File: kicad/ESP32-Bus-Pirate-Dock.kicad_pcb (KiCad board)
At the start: 2 copper layers, 95.3 x 74.8 mm, 21 parts, among them J1 Conn_01x10V, J2 Conn_01x22, J3 Conn_01x22, J4 Conn_01x10H, U1 ESP32-S3-DEVKITC-1-N8R2, U2 AMS1117-1.8, U3 FXMA108

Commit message: Added logo
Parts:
- added G***: LOGO, LOGO, F.Cu at (193.8, 116.0)
- SW_1: value SW_BOOT -> BOOT
- moved C3 51.5 mm to (192.6, 90.2)
- moved C2 49.2 mm to (189.2, 86.4)
- moved U2 49.2 mm to (194.8, 83.6)
- moved C1 47.5 mm to (196.6, 90.2), turned to 0 degrees
- moved C4 45.1 mm to (189.2, 81.2), turned to 90 degrees
- moved H2 10.1 mm to (205.0, 53.8)
- moved H4 10.1 mm to (205.4, 120.1)
- moved D2 8.90 mm to (188.3, 62.5)
- moved S1 8.90 mm to (188.2, 54.7)
- moved D1 8.90 mm to (192.4, 62.5)
- moved D3 8.90 mm to (184.2, 62.5)
- moved R1 8.90 mm to (198.6, 56.6)
- moved SW_1 7.01 mm to (194.6, 105.3)
- moved U1 2.46 mm to (162.2, 93.3)
- moved U3 2.46 mm to (138.4, 90.9)
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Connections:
- U3 pad 11: unconnected-(U3-~{OE}-Pad11) -> GND
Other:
- board size 95.3 x 74.8 mm -> 85.4 x 74.8 mm

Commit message: First wiring attempt
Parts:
- moved H1 10.6 mm to (129.3, 64.4)
- moved R1 10.6 mm to (198.5, 67.2)
- moved H2 10.6 mm to (204.9, 64.4)
- moved S1 10.6 mm to (188.1, 65.2)
- moved D1 10.4 mm to (192.4, 72.9)
- moved D2 10.4 mm to (188.3, 72.9)
- moved D3 10.4 mm to (184.2, 72.9)
- moved G*** 3.56 mm to (192.2, 119.1)
- moved J3 0.91 mm to (146.9, 63.3)
- moved H3 0.68 mm to (129.1, 120.4)
- moved J2 0.64 mm to (177.4, 63.3)
- moved H4 0.14 mm to (205.3, 120.2)
- moved J4 0.09 mm to (127.2, 80.7)
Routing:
- net +5V: track 0.00 -> 93.6 mm
- net VTARGET: track 0.00 -> 91.0 mm, vias 0 -> 2
- net +1V8: track 0.00 -> 35.6 mm
- net GPIO0: track 0.00 -> 26.7 mm
- net GPIO13: track 0.00 -> 23.2 mm
- net GPIO12: track 0.00 -> 22.0 mm
- net GPIO11: track 0.00 -> 19.9 mm
- net GPIO10: track 0.00 -> 18.7 mm
- net IO13: track 0.00 -> 15.5 mm
- net GPIO15: track 0.00 -> 15.2 mm
- net IO12: track 0.00 -> 13.8 mm
- net GPIO16: track 0.00 -> 13.6 mm
- net IO15: track 0.00 -> 13.0 mm
- net GPIO17: track 0.00 -> 12.7 mm
- net GPIO18: track 0.00 -> 11.9 mm
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- added copper zone on B.Cu, net +3.3V
- added copper zone on F.Cu, net +3.3V
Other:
- board size 85.4 x 74.8 mm -> 85.4 x 64.8 mm

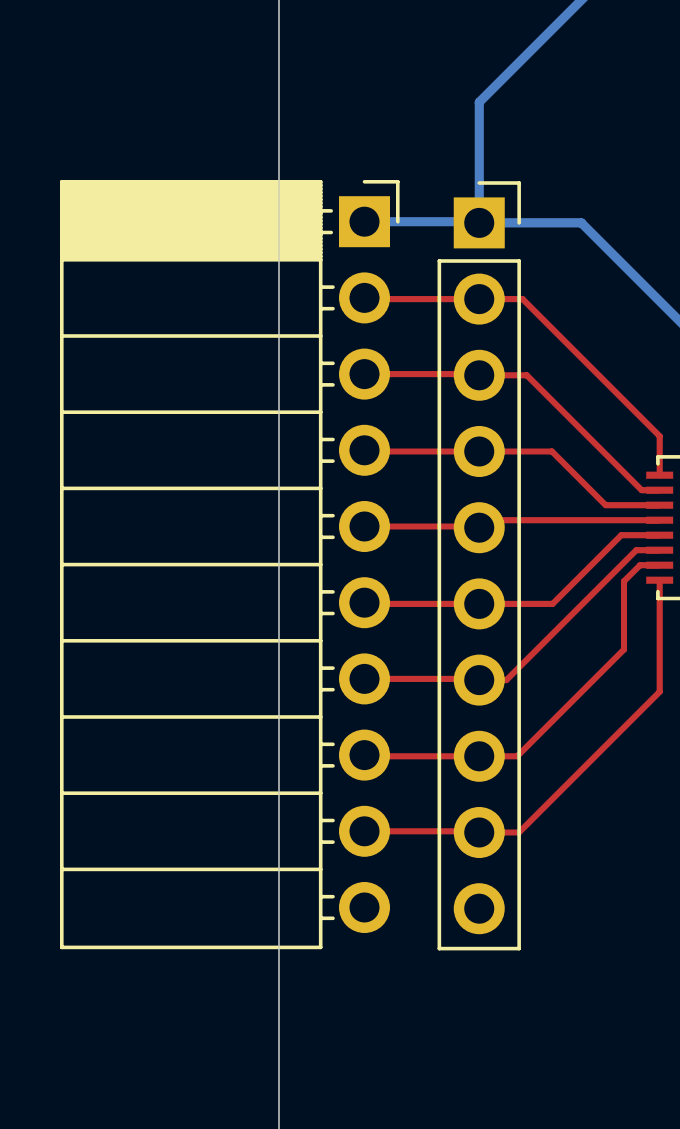
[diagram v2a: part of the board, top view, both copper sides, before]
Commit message: Excluded vertical header
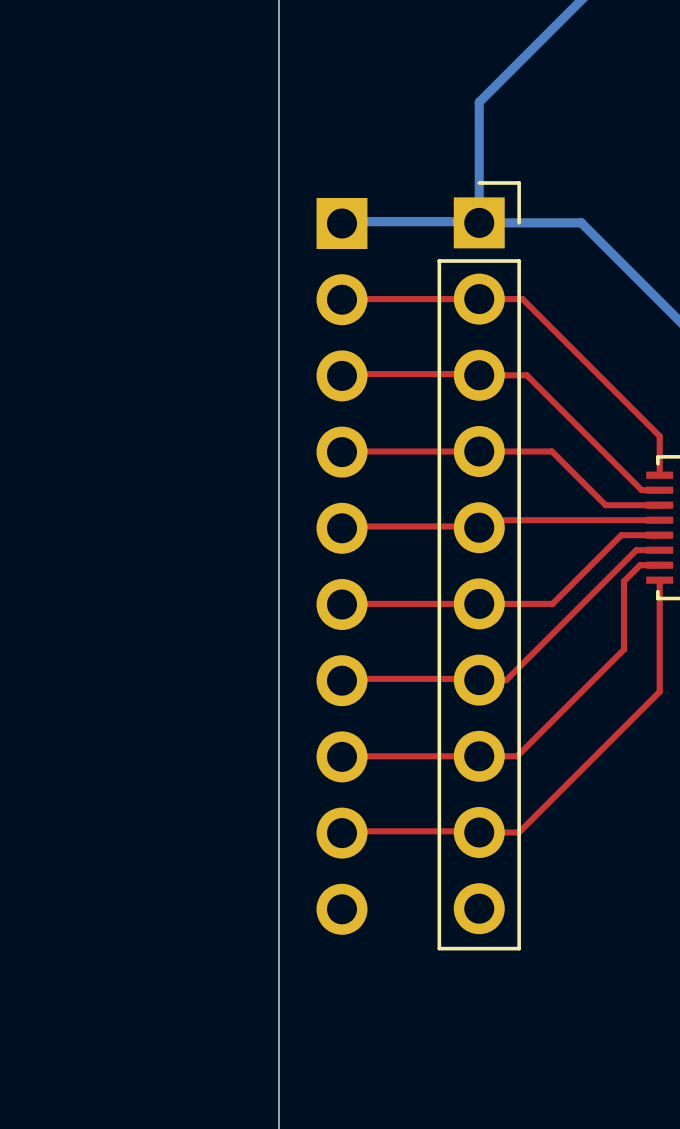
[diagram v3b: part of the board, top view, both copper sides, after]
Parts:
- J4: footprint Connector_PinSocket_2.54mm:PinSocket_1x10_P2.54mm_Horizontal -> Connector_PinHeader_2.54mm:PinHeader_1x10_P2.54mm_Horizontal; moved to B.Cu
- SW_1: value BOOT -> SW_BOOT
- moved J4 0.75 mm to (126.5, 80.8), turned to 180 degrees

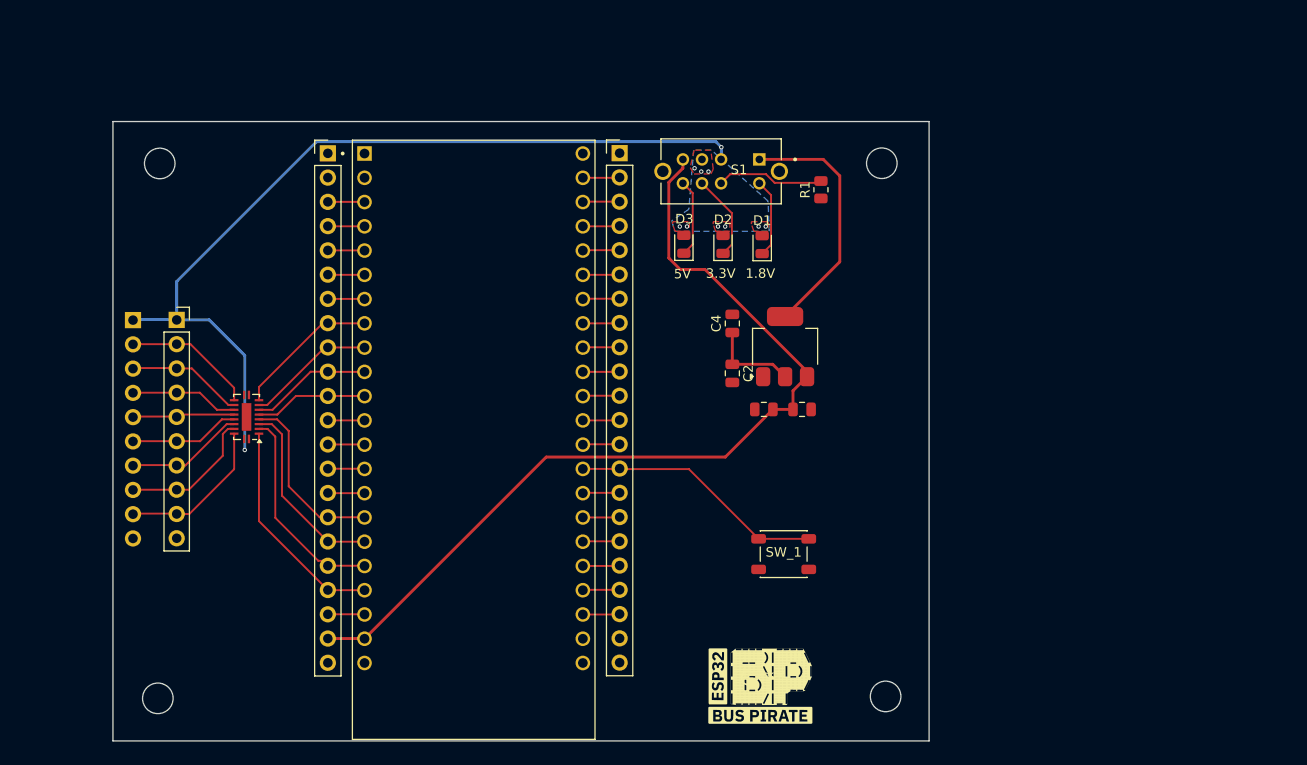
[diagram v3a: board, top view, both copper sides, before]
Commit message: Added keyed connector
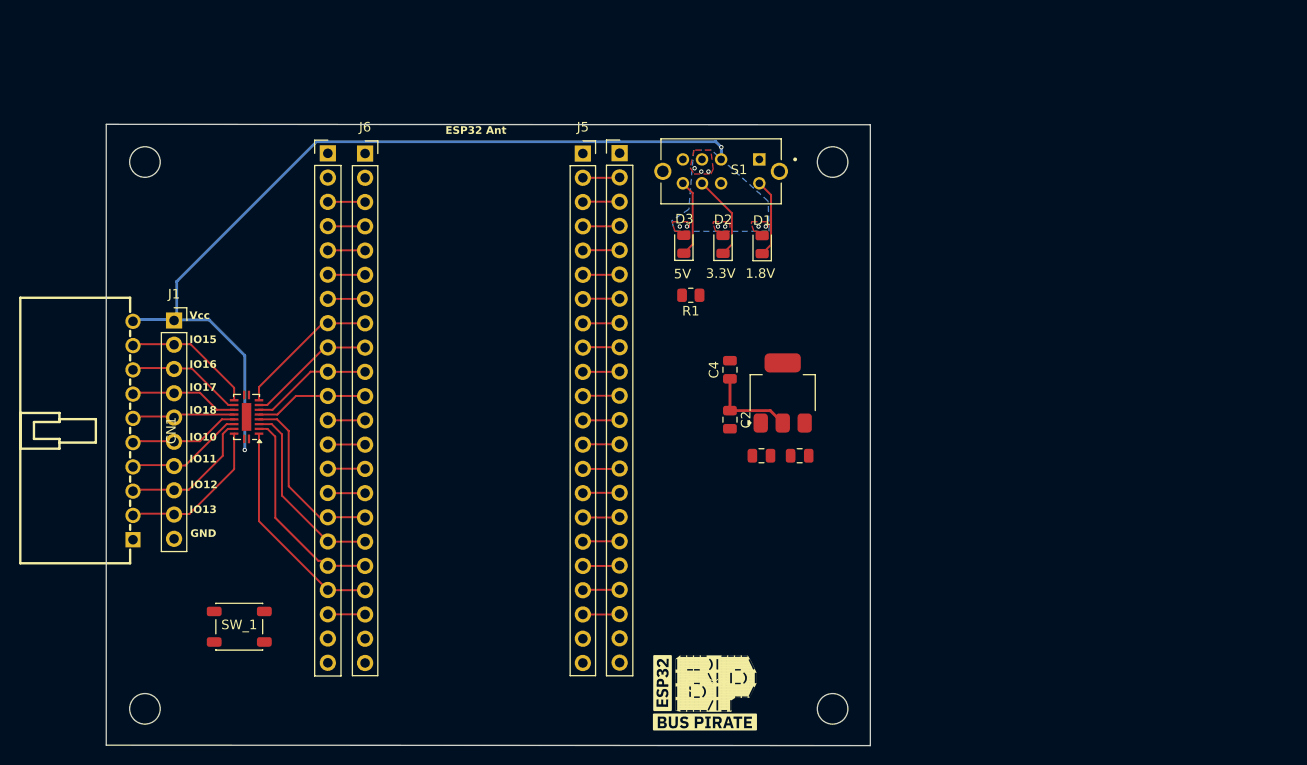
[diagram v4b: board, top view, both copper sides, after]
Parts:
- removed J4: Conn_01x10H, Connector_PinHeader_2.54mm:PinHeader_1x10_P2.54mm_Horizontal
- removed U1: ESP32-S3-DEVKITC-1-N8R2, ESP32-S3-DEVKITC-1-N8R2:XCVR_ESP32-S3-DEVKITC-1-N8R2
- added CN1: HX25418-10WA, HX25418:CONN-TH_HX25418-10WA, F.Cu at (126.5, 92.4)
- added J5: Conn_01x22, Connector_PinSocket_2.54mm:PinSocket_1x22_P2.54mm_Vertical, F.Cu at (173.6, 63.4)
- added J6: Conn_01x22, Connector_PinSocket_2.54mm:PinSocket_1x22_P2.54mm_Vertical, F.Cu at (150.8, 63.4)
- moved SW_1 57.5 mm to (137.6, 112.9)
- moved R1 17.5 mm to (184.9, 78.2), turned to 180 degrees
- moved G*** 5.84 mm to (186.4, 119.8)
- moved H4 5.70 mm to (199.8, 121.5)
- moved H2 5.15 mm to (199.8, 64.2)
- moved C1 4.86 mm to (196.3, 95.0)
- moved C2 4.86 mm to (189.0, 91.2)
- moved C3 4.86 mm to (192.3, 95.0)
- moved C4 4.86 mm to (189.0, 86.0)
- moved U2 4.86 mm to (194.5, 88.4)
- moved H3 1.74 mm to (127.8, 121.5)
- moved H1 1.56 mm to (127.8, 64.2)
- moved J1 0.28 mm to (130.8, 80.8)
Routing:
- net +5V: track 93.6 -> 0.00 mm
- net +1V8: track 35.6 -> 9.39 mm
- net GPIO0: track 26.7 -> 3.95 mm
- net Net-(R1-Pad2): track 11.3 -> 0.00 mm
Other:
- board size 85.4 x 64.8 mm -> 80 x 65 mm
- board text added: "ESP32 Ant"
- board text added: "GND"
- board text added: "IO10"
- board text added: "IO11"
- board text added: "IO12"
- board text added: "IO13"
- board text added: "IO15"
- board text added: "IO16"
- board text added: "IO17"
- board text added: "IO18"
- board text added: "Vcc"

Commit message: Fully routed PCB prototype
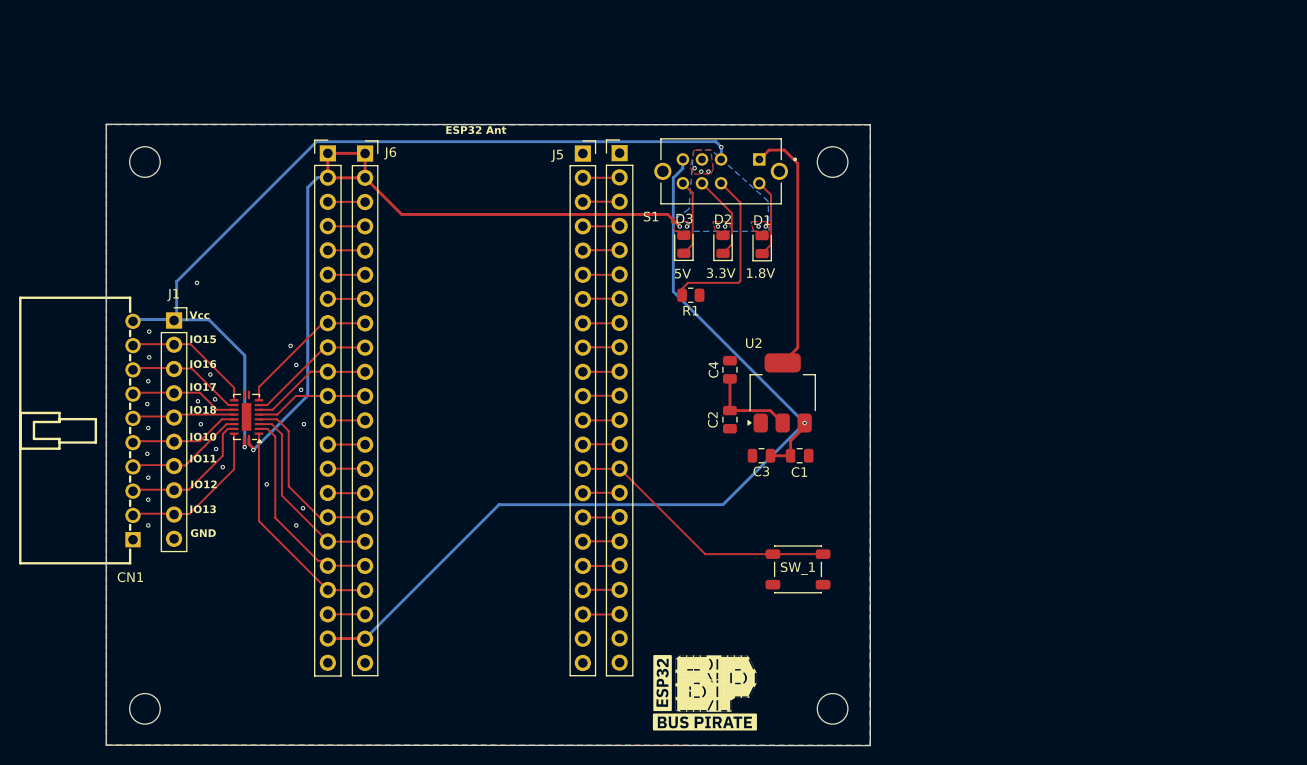
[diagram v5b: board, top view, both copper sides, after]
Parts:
- moved SW_1 58.8 mm to (196.1, 106.9)
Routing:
- net +5V: track 0.00 -> 99.1 mm, vias 0 -> 1
- net +3.3V: track 0.00 -> 81.7 mm, vias 9 -> 10
- net +1V8: track 9.39 -> 35.9 mm
- net GPIO0: track 3.95 -> 28.9 mm
- net Net-(R1-Pad2): track 0.00 -> 18.2 mm
- net VTARGET: track 91.0 -> 91.6 mm
- net GND: vias 0 -> 23
- added copper zone on B.Cu, net GND
- added copper zone on F.Cu, net GND

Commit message: DRC Check Passed
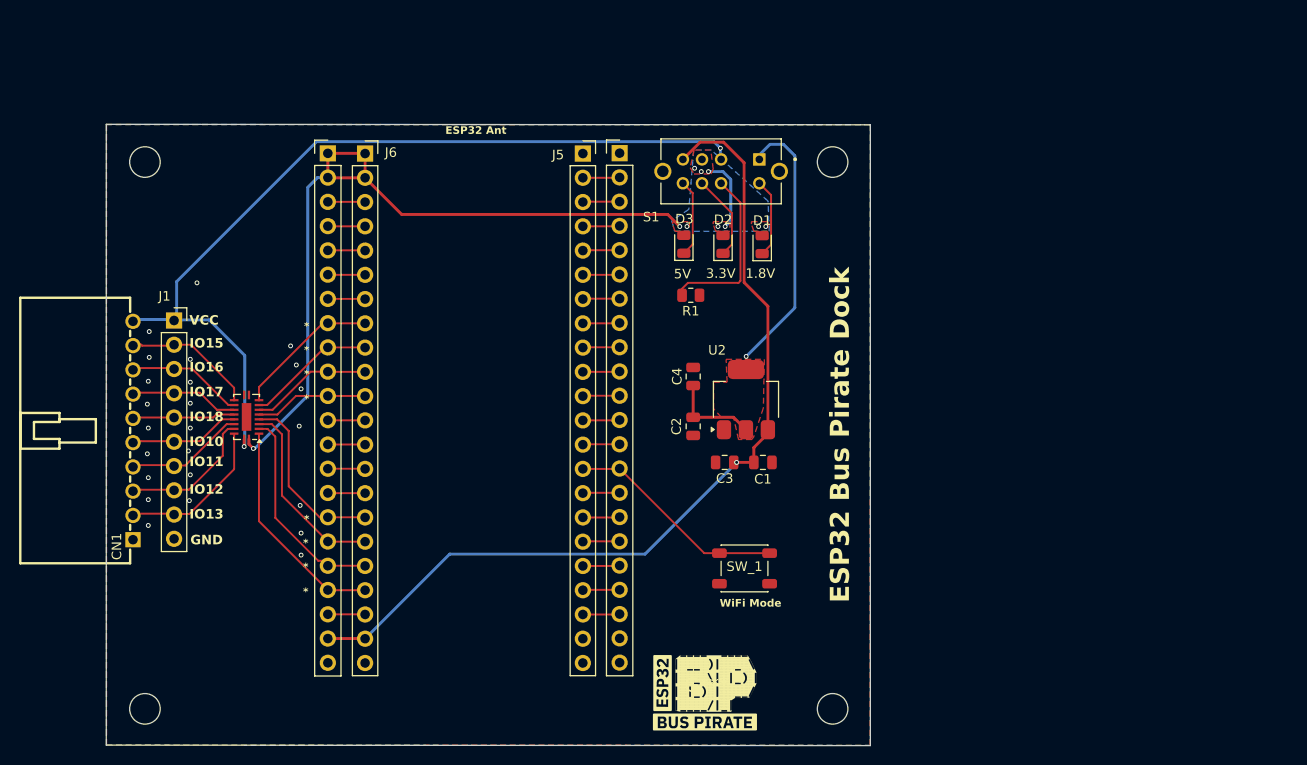
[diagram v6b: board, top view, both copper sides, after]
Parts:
- moved SW_1 5.60 mm to (190.5, 106.8)
- moved C1 3.91 mm to (192.4, 95.7)
- moved C3 3.91 mm to (188.4, 95.7)
- moved C2 3.91 mm to (185.2, 91.9)
- moved C4 3.91 mm to (185.2, 86.7)
- moved U2 3.91 mm to (190.7, 89.1)
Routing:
- net +3.3V: track 81.7 -> 89.3 mm
- net GPIO0: track 28.9 -> 23.2 mm
- net +5V: track 99.1 -> 93.6 mm
- net +1V8: track 35.9 -> 39.0 mm, vias 0 -> 1
- net IO18: track 9.96 -> 10.8 mm
- net GND: vias 23 -> 24
- added copper zone on F.Cu, net +1V8
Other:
- board text added: "*"
- board text added: "ESP32 Bus Pirate Dock"
- board text added: "VCC"
- board text added: "WiFi Mode"
- board text removed: "Vcc"

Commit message: Fixed connector polarity
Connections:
- CN1 pad 1: GND -> VTARGET
- CN1 pad 10: VTARGET -> GND
- J1 pad 1: VTARGET -> GND
- J1 pad 10: GND -> VTARGET
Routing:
- net VTARGET: track 91.4 -> 99.6 mm, vias 2 -> 1
- net GND: vias 24 -> 30
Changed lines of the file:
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@@
 			(layers "*.Cu" "*.Mask")
 			(remove_unused_layers no)
-			(net 10 "GND")
+			(net 43 "VTARGET")
 			(pinfunction "1")
 			(pintype "unspecified")
@@
 			(layers "*.Cu" "*.Mask")
 			(remove_unused_layers no)
-			(net 43 "VTARGET")
+			(net 10 "GND")
 			(pinfunction "10")
 			(pintype "unspecified")
@@
 			(layers "*.Cu" "*.Mask")
 			(remove_unused_layers no)
-			(net 43 "VTARGET")
+			(net 10 "GND")
 			(pinfunction "Pin_1")
 			(pintype "passive")
@@
 			(layers "*.Cu" "*.Mask")
 			(remove_unused_layers no)
-			(net 10 "GND")
+			(net 43 "VTARGET")
 			(pinfunction "Pin_10")
 			(pintype "passive")
@@
 	)
 	(gr_text "GND"
-		(at 132.5 104.4 0)
+		(at 132.5 81.5 0)
 		(layer "F.SilkS")
 		(effects
@@
 	)
 	(gr_text "VCC"
-		(at 132.4 81.4 0)
+		(at 132.5 104.1 0)
 		(layer "F.SilkS")
 		(effects
@@
 	)
 	(via
+		(at 157.3 66.6)
+		(size 0.5032)
+		(drill 0.3)
+		(layers "F.Cu" "B.Cu")
+		(free yes)
+		(net 10)
+	)
+	(via
 		(at 144 100.2)
 		(size 0.5032)
@@
 	)
 	(via
+		(at 169.2 62.8)
+		(size 0.5032)
+		(drill 0.3)
+		(layers "F.Cu" "B.Cu")
+		(free yes)
+		(net 10)
+	)
+	(via
 		(at 144.1 105.4)
 		(size 0.5032)
@@
 	)
 	(via
+		(at 156.8 100.1)
+		(size 0.5032)
+		(drill 0.3)
+		(layers "F.Cu" "B.Cu")
+		(free yes)
+		(net 10)
+	)
+	(via
 		(at 128.1 92.1)
 		(size 0.5032)
@@
 	)
 	(via
+		(at 156.015796 82.394434)
+		(size 0.5032)
+		(drill 0.3)
+		(layers "F.Cu" "B.Cu")
+		(free yes)
+		(net 10)
+	)
+	(via
 		(at 132.5 84.9)
 		(size 0.5032)
@@
 	)
 	(via
+		(at 168.8 72.1)
+		(size 0.5032)
+		(drill 0.3)
+		(layers "F.Cu" "B.Cu")
+		(free yes)
+		(net 10)
+	)
+	(via
+		(at 168.5 90.9)
+		(size 0.5032)
+		(drill 0.3)
+		(layers "F.Cu" "B.Cu")
+		(free yes)
+		(net 10)
+	)
+	(via
 		(at 143.9 91.9)
 		(size 0.5032)
@@
 	)
 	(segment
-		(start 138.14 94.04)
-		(end 138.14 93.24)
+		(start 126.59 103.7)
+		(end 126.5 103.79)
 		(width 0.3048)
 		(layer "F.Cu")
 		(net 43)
 	)
-	(via
-		(at 138.14 94.04)
-		(size 0.5032)
-		(drill 0.3)
-		(layers "F.Cu" "B.Cu")
-		(free yes)
-		(net 43)
-	)
-	(via
-		(at 188 62.8)
-		(size 0.5032)
-		(drill 0.3)
-		(layers "F.Cu" "B.Cu")
-		(free yes)
+	(segment
+		(start 138.14 101.96)
+		(end 138.14 96.2)
+		(width 0.3048)
+		(layer "F.Cu")
 		(net 43)
 	)
 	(segment
-		(start 188 63.9)
-		(end 188.075 63.975)
+		(start 136.4 103.7)
+		(end 138.14 101.96)
 		(width 0.3048)
-		(layer "B.Cu")
+		(layer "F.Cu")
 		(net 43)
 	)
 	(segment
-		(start 138.14 94.04)
-		(end 138.2 93.98)
+		(start 130.8 103.7)
+		(end 126.59 103.7)
 		(width 0.3048)
-		(layer "B.Cu")
+		(layer "F.Cu")
 		(net 43)
 	)
 	(segment
-		(start 188 62.8)
-		(end 188 63.9)
+		(start 130.8 103.7)
+		(end 136.4 103.7)
 		(width 0.3048)
-		(layer "B.Cu")
+		(layer "F.Cu")
 		(net 43)
 	)
 	(segment
-		(start 138.2 93.98)
-		(end 138.2 84.5)
+		(start 138.14 96.2)
+		(end 138.14 93.24)
 		(width 0.3048)
-		(layer "B.Cu")
+		(layer "F.Cu")
+		(net 43)
+	)
+	(via
+		(at 138.14 96.2)
+		(size 0.5032)
+		(drill 0.3)
+		(layers "F.Cu" "B.Cu")
 		(net 43)
 	)
 	(segment
-		(start 138.2 84.5)
-		(end 134.48 80.78)
+		(start 138.14 96.2)
+		(end 138.14 71.76)
 		(width 0.3048)
 		(layer "B.Cu")
@@
 	)
 	(segment
-		(start 145.7166 62.1166)
-		(end 131.075 76.7582)
+		(start 182.459824 62.9676)
+		(end 187.0676 62.9676)
 		(width 0.3048)
 		(layer "B.Cu")
@@
 	)
 	(segment
-		(start 131.075 76.7582)
-		(end 131.075 80.78)
+		(start 180.904024 64.5234)
+		(end 182.459824 62.9676)
 		(width 0.3048)
 		(layer "B.Cu")
@@
 	)
 	(segment
-		(start 187.3166 62.1166)
-		(end 145.7166 62.1166)
+		(start 176.2466 64.5234)
+		(end 180.904024 64.5234)
 		(width 0.3048)
 		(layer "B.Cu")
@@
 	)
 	(segment
-		(start 134.48 80.78)
-		(end 131.075 80.78)
+		(start 176.0934 64.6766)
+		(end 176.2466 64.5234)
 		(width 0.3048)
 		(layer "B.Cu")
@@
 	)
 	(segment
-		(start 131.035 80.74)
-		(end 131.075 80.78)
+		(start 138.14 71.76)
+		(end 145.2234 64.6766)
 		(width 0.3048)
 		(layer "B.Cu")
@@
 	)
 	(segment
-		(start 127.25 80.74)
-		(end 131.035 80.74)
+		(start 187.0676 62.9676)
+		(end 188.075 63.975)
 		(width 0.3048)
 		(layer "B.Cu")
@@
 	)
 	(segment
-		(start 188 62.8)
-		(end 187.3166 62.1166)
+		(start 145.2234 64.6766)
+		(end 176.0934 64.6766)
 		(width 0.3048)
 		(layer "B.Cu")

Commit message: Modified for PCBWay prototype
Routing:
- net GND: vias 30 -> 31
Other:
- board text added: "WayWayWay"
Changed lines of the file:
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@@
 			(drillshape 0)
 			(scaleselection 1)
-			(outputdirectory "/home/admin-andrei/Downloads/test/")
+			(outputdirectory "/home/admin-andrei/Downloads/esp32_bus_pirate_dock_outputs/")
 		)
 	)
@@
 		)
 	)
+	(gr_text "WayWayWay"
+		(at 171 116.8 90)
+		(layer "F.SilkS")
+		(effects
+			(font
+				(size 0.8 0.8)
+				(thickness 0.15)
+				(bold yes)
+			)
+			(justify left bottom)
+		)
+	)
 	(gr_text "ESP32 Bus Pirate Dock"
 		(at 201.7 110.4 90)
@@
 		(size 0.5032)
 		(drill 0.3)
+		(layers "F.Cu" "B.Cu")
+		(free yes)
+		(net 10)
+	)
+	(via
+		(at 136.5 101.2)
+		(size 0.5032)
+		(drill 0.3)
